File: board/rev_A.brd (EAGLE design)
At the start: 15 x 30 mm, 25 parts, among them IC1 STM32F303K8T, IC2 MCP6292, U1 V_REG_LDOSMD, U2 V_REG_LDOSMD

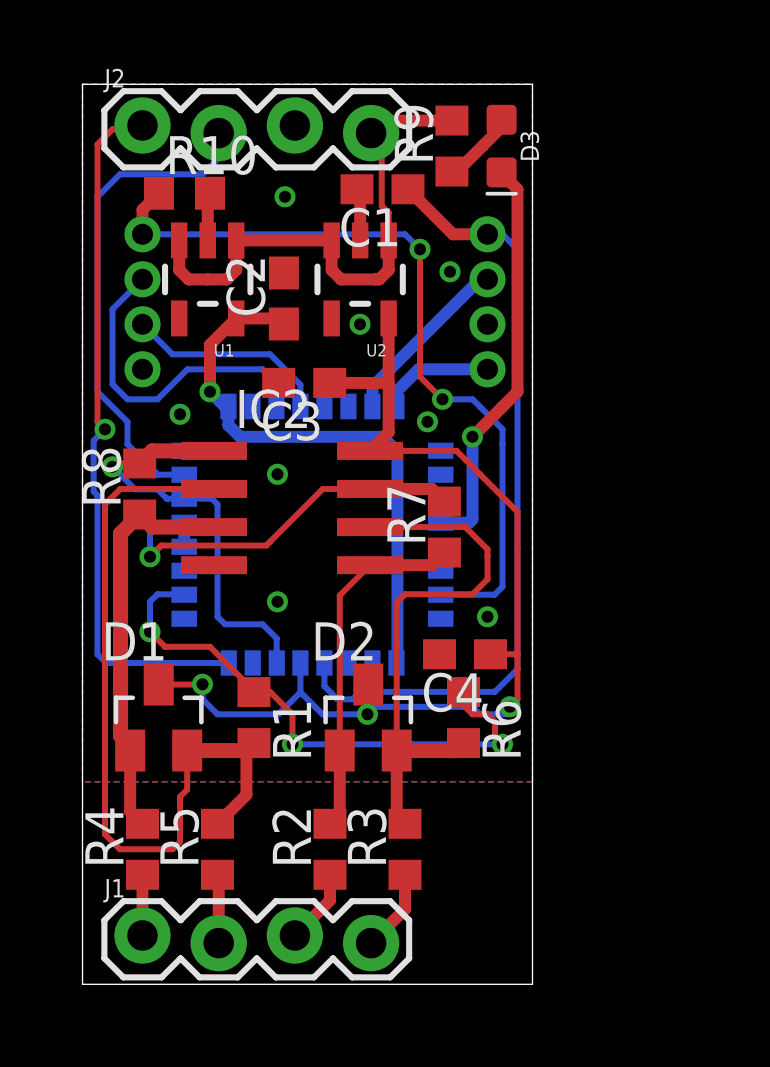
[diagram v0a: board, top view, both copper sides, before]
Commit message: [Boards] Adding bypass cap and optimizing routing.
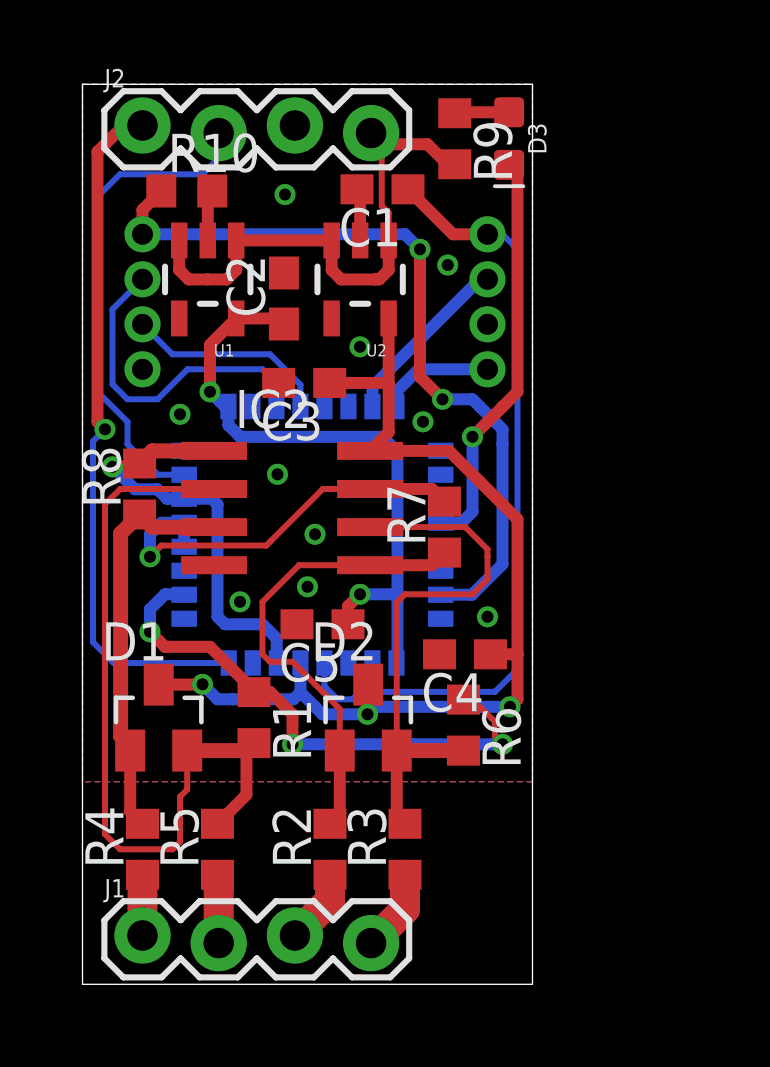
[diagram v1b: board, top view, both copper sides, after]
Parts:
- added C5: 2.2uF, resistor:C0603
- moved D3 0.35 mm to (14.2, 28.2)
- moved R9 0.26 mm to (12.4, 28.2), turned to 270 degrees
- moved R6 0.25 mm to (12.7, 8.64)
- moved R10 0.11 mm to (3.48, 26.4)
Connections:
- net +3V3: now also C5.1
- net GND: now also C5.2
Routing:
- net N$1: track 11.8 -> 15.8 mm
- net +3V3: track 19.0 -> 21.4 mm, vias 1 -> 2
- net VDDA: track 35.3 -> 34.2 mm
- net N$5: track 2.51 -> 1.82 mm
- net N$4: track 13.5 -> 14.2 mm
- net GND: track 3.32 -> 3.43 mm, vias 8 -> 10

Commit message: [Board] Prepping for panels, cleaning labels, adding optional shunt resistors.
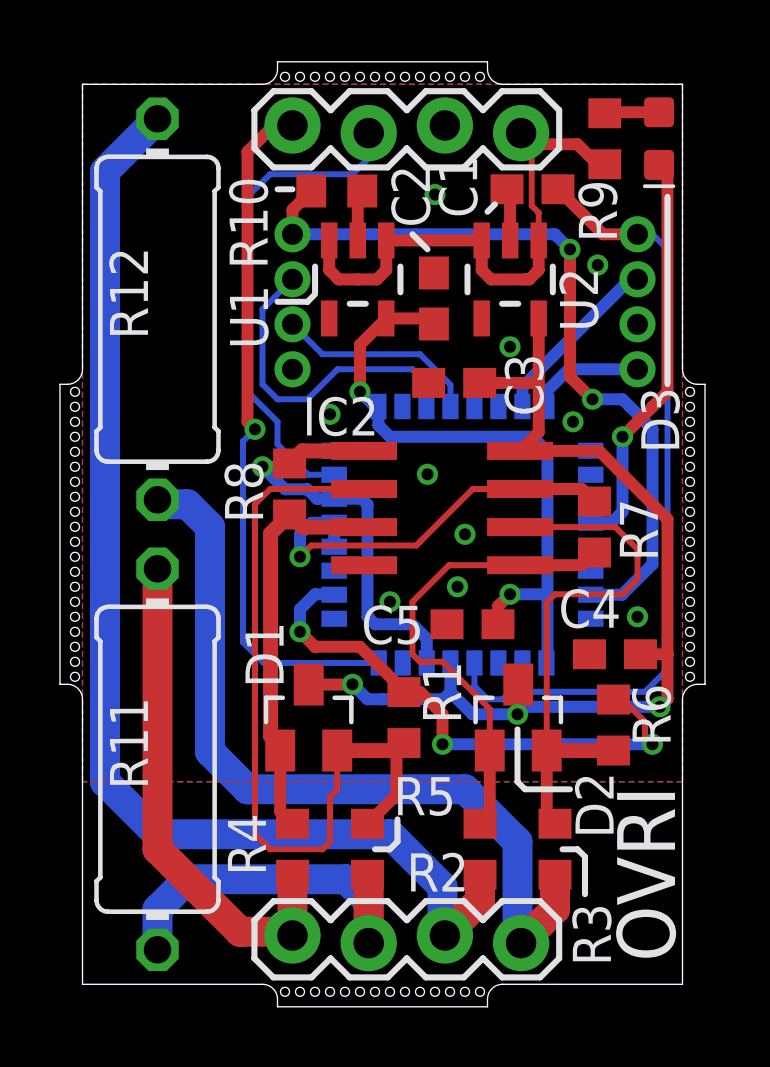
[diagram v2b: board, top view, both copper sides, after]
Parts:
- added R11, R12: 5K, resistor:0411/12
- moved R7 5.00 mm to (17.1, 15.2)
- moved C3 5.00 mm to (12.4, 20.0)
- moved R10 5.00 mm to (8.48, 26.4)
- moved U1 5.00 mm to (9.18, 23.5)
- moved C1 5.00 mm to (15.0, 26.5)
- moved C2 5.00 mm to (11.7, 22.9)
- moved C4 5.00 mm to (17.8, 11.0)
- moved C5 5.00 mm to (13.0, 12.0)
- moved D1 5.00 mm to (7.54, 8.89)
- moved D2 5.00 mm to (14.5, 8.89)
- moved J1 5.00 mm to (7.00, 1.50)
- moved J2 5.00 mm to (7.00, 28.5)
- moved J_DBG 5.00 mm to (18.5, 22.8)
- moved J_SER 5.00 mm to (7.00, 22.8)
- moved R1 5.00 mm to (10.7, 8.89)
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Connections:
- net VR1+: now also R11.1
- net VR1-: now also R11.2
- net VR2+: now also R12.1
- net VR2-: now also R12.2
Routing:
- net VR2+: track 2.51 -> 39.7 mm
- net VR2-: track 2.75 -> 27.3 mm
- net VR1+: track 2.02 -> 17.1 mm
- net VR1-: track 2.29 -> 12.8 mm
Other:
- board size 15 x 30 mm -> 21.5 x 31.5 mm
- board text added: "BOOT0"
- board text added: "GND"
- board text added: "OVRI"
- board text added: "RX"
- board text added: "Rev A"
- board text added: "TX"
